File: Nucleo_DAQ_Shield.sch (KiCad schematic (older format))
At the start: 23 parts, among them J1 CONN_01X02, J2 CONN_COAXIAL, J3 CONN_01X06, J4 CONN_01X02, J5 CONN_01X06, U1 TL072, U2 7805, U3 TLV70233DBV, U4 4050

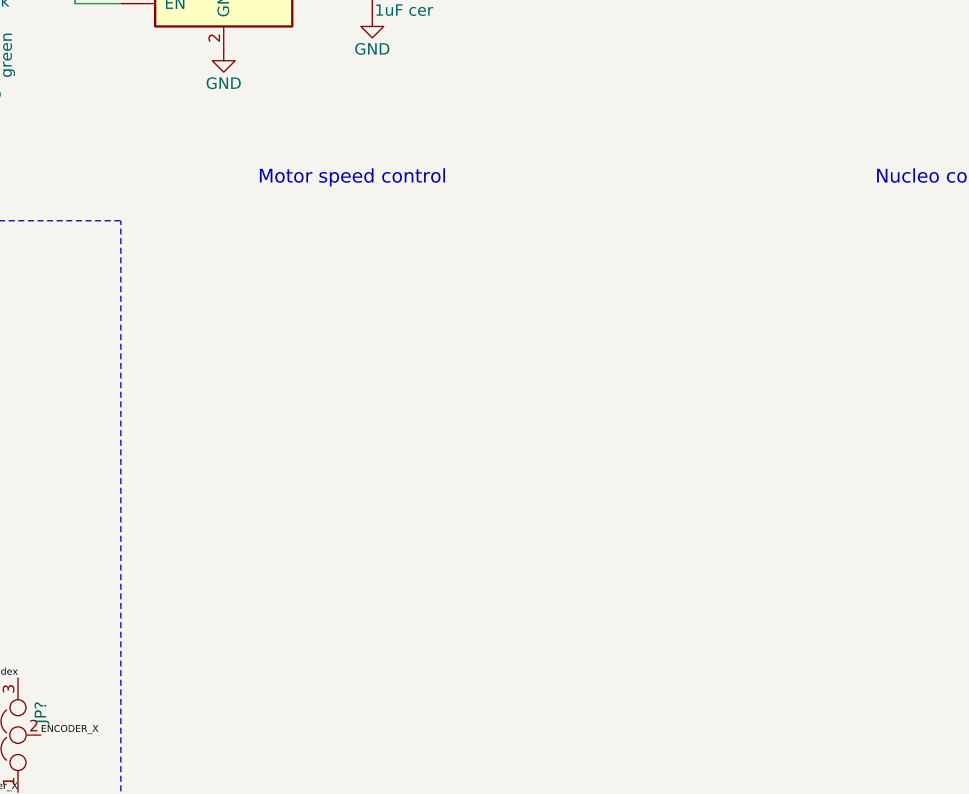
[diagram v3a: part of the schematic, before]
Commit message: Added H-bridge for motor speed control
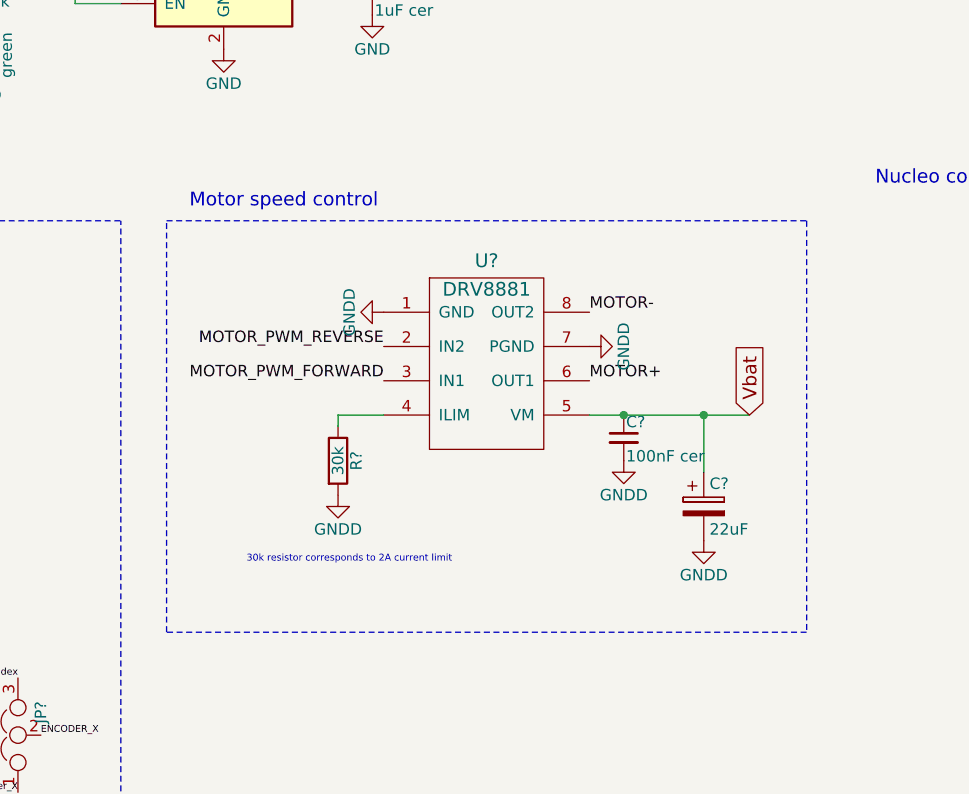
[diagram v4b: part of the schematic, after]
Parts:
- added C?: 22uF, symbol CP
- added C?: 100nF cer, symbol C_Small
- added R?: 30k, symbol R
- added U?: DRV8881, symbol DRV8881
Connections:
- net GND: now also C?.2, C?.2, R?.2, U?.1 (GND), U?.7 (PGND)
- net MOTOR+: now also U?.6 (OUT1)
- net MOTOR-: now also U?.8 (OUT2)
- net Vbat: now also C?.1, C?.1, U?.5 (VM)
- new net: R?.1, U?.4 (ILIM)
- new net MOTOR_PWM_FORWARD: U?.3 (IN1)
- new net MOTOR_PWM_REVERSE: U?.2 (IN2)
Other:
- note added: "30k resistor corresponds to 2A current limit"
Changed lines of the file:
@@
 LIBS:contrib
 LIBS:valves
+LIBS:DRV8881
 LIBS:Nucleo_DAQ_Shield-cache
 EELAYER 25 0
@@
 Text Label 4450 4350 0    30   ~ 0
 ENCODER_B
-Text Notes 6100 1950 0    60   ~ 0
+Text Notes 5800 2050 0    60   ~ 0
 Motor speed control
 Text Notes 8800 1950 0    60   ~ 0
@@
 Wire Notes Line
 	5500 5100 5500 2100
+$Comp
+L DRV8881 U?
+U 1 1 595E1ABC
+P 7100 2750
+F 0 "U?" H 7100 3225 60  0000 C CNN
+F 1 "DRV8881" H 7100 3100 60  0000 C CNN
+F 2 "" H 7100 2750 60  0001 C CNN
+F 3 "" H 7100 2750 60  0001 C CNN
+	1    7100 2750
+	1    0    0    -1
+$EndComp
+$Comp
+L GNDD #PWR?
+U 1 1 595E2075
+P 6650 2500
+F 0 "#PWR?" H 6650 2250 50  0001 C CNN
+F 1 "GNDD" H 6650 2350 50  0000 C CNN
+F 2 "" H 6650 2500 50  0001 C CNN
+F 3 "" H 6650 2500 50  0001 C CNN
+	1    6650 2500
+	0    1    1    0
+$EndComp
+$Comp
+L GNDD #PWR?
+U 1 1 595E228B
+P 7550 2650
+F 0 "#PWR?" H 7550 2400 50  0001 C CNN
+F 1 "GNDD" H 7550 2500 50  0000 C CNN
+F 2 "" H 7550 2650 50  0001 C CNN
+F 3 "" H 7550 2650 50  0001 C CNN
+	1    7550 2650
+	0    -1   -1   0
+$EndComp
+$Comp
+L CP C?
+U 1 1 595E27CD
+P 8050 3350
+F 0 "C?" H 8075 3450 50  0000 L CNN
+F 1 "22uF" H 8075 3250 50  0000 L CNN
+F 2 "" H 8088 3200 50  0001 C CNN
+F 3 "" H 8050 3350 50  0001 C CNN
+	1    8050 3350
+	1    0    0    -1
+$EndComp
+Text GLabel 8250 2950 1    60   Input ~ 0
+Vbat
+$Comp
+L R R?
+U 1 1 595E2B28
+P 6450 3150
+F 0 "R?" V 6530 3150 50  0000 C CNN
+F 1 "30k" V 6450 3150 50  0000 C CNN
+F 2 "" V 6380 3150 50  0001 C CNN
+F 3 "" H 6450 3150 50  0001 C CNN
+	1    6450 3150
+	1    0    0    -1
+$EndComp
+$Comp
+L GNDD #PWR?
+U 1 1 595E2DB5
+P 6450 3300
+F 0 "#PWR?" H 6450 3050 50  0001 C CNN
+F 1 "GNDD" H 6450 3150 50  0000 C CNN
+F 2 "" H 6450 3300 50  0001 C CNN
+F 3 "" H 6450 3300 50  0001 C CNN
+	1    6450 3300
+	1    0    0    -1
+$EndComp
+Wire Wire Line
+	6650 2950 6450 2950
+Wire Wire Line
+	6450 2950 6450 3000
+Text Label 7550 2800 0    50   ~ 0
+MOTOR+
+Text Label 7550 2500 0    50   ~ 0
+MOTOR-
+$Comp
+L C_Small C?
+U 1 1 595E32FF
+P 7700 3050
+F 0 "C?" H 7710 3120 50  0000 L CNN
+F 1 "100nF cer" H 7710 2970 50  0000 L CNN
+F 2 "" H 7700 3050 50  0001 C CNN
+F 3 "" H 7700 3050 50  0001 C CNN
+	1    7700 3050
+	1    0    0    -1
+$EndComp
+$Comp
+L GNDD #PWR?
+U 1 1 595E3B16
+P 7700 3150
+F 0 "#PWR?" H 7700 2900 50  0001 C CNN
+F 1 "GNDD" H 7700 3000 50  0000 C CNN
+F 2 "" H 7700 3150 50  0001 C CNN
+F 3 "" H 7700 3150 50  0001 C CNN
+	1    7700 3150
+	1    0    0    -1
+$EndComp
+$Comp
+L GNDD #PWR?
+U 1 1 595E3B7B
+P 8050 3500
+F 0 "#PWR?" H 8050 3250 50  0001 C CNN
+F 1 "GNDD" H 8050 3350 50  0000 C CNN
+F 2 "" H 8050 3500 50  0001 C CNN
+F 3 "" H 8050 3500 50  0001 C CNN
+	1    8050 3500
+	1    0    0    -1
+$EndComp
+Wire Wire Line
+	7550 2950 8250 2950
+Connection ~ 7700 2950
+Connection ~ 8050 2950
+Text Label 6650 2800 2    50   ~ 0
+MOTOR_PWM_FORWARD
+Text Label 6650 2650 2    50   ~ 0
+MOTOR_PWM_REVERSE
+Wire Wire Line
+	8050 3200 8050 2950
+Text Notes 6050 3600 0    30   ~ 0
+30k resistor corresponds to 2A current limit
+Wire Notes Line
+	5700 2100 8500 2100
+Wire Notes Line
+	8500 2100 8500 3900
+Wire Notes Line
+	8500 3900 5700 3900
+Wire Notes Line
+	5700 3900 5700 2100
 $EndSCHEMATC

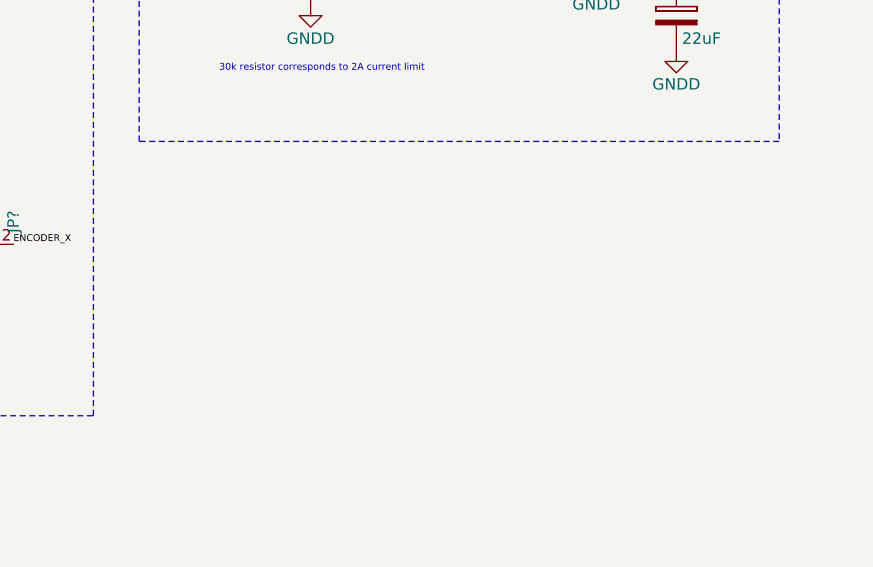
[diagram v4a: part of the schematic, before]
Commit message: Added reference diagram for the electrical characteristics of the ADC input
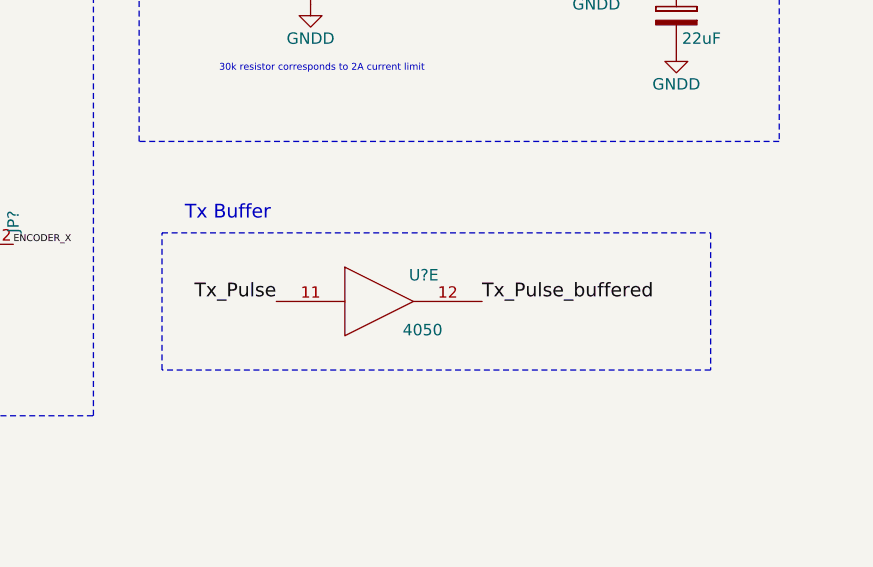
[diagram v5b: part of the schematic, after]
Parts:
- added U?: 4050, symbol 4050
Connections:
- net +3.3VA: now also U?.1 (VCC)
- net GND: now also U?.8 (VSS)
- new net Tx_Pulse: U?.11
- new net Tx_Pulse_buffered: U?.12
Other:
- note added: "Tx Buffer"

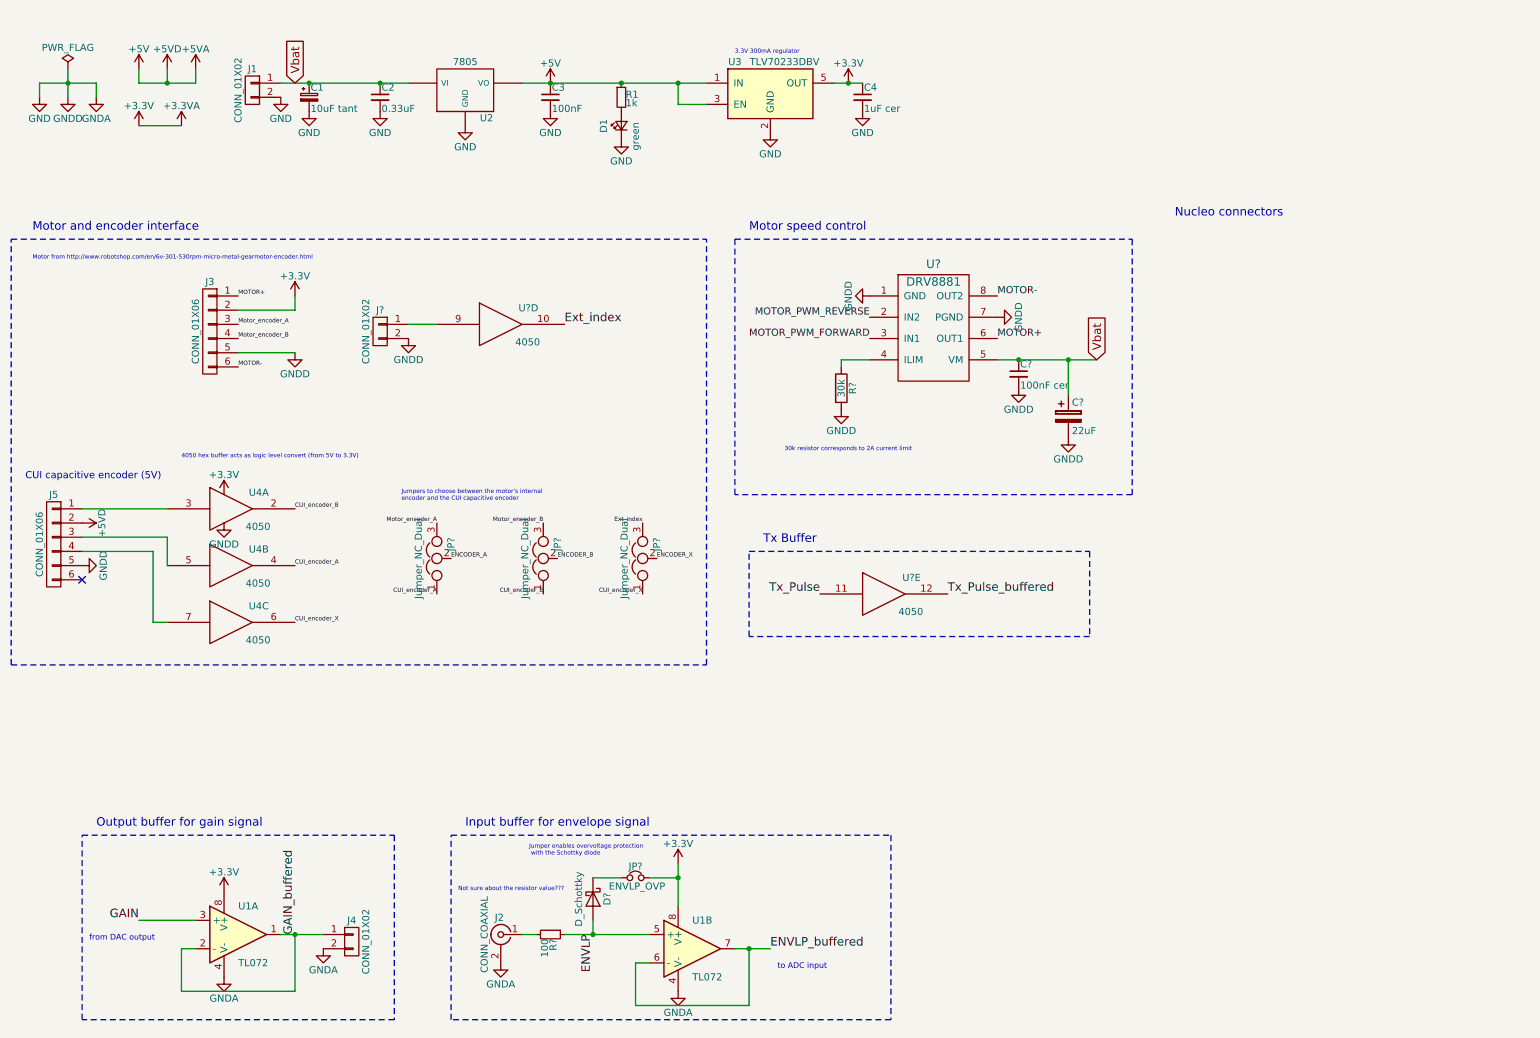
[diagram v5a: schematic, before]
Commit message: Added Nucleo connectors to schematic and started associating footprints
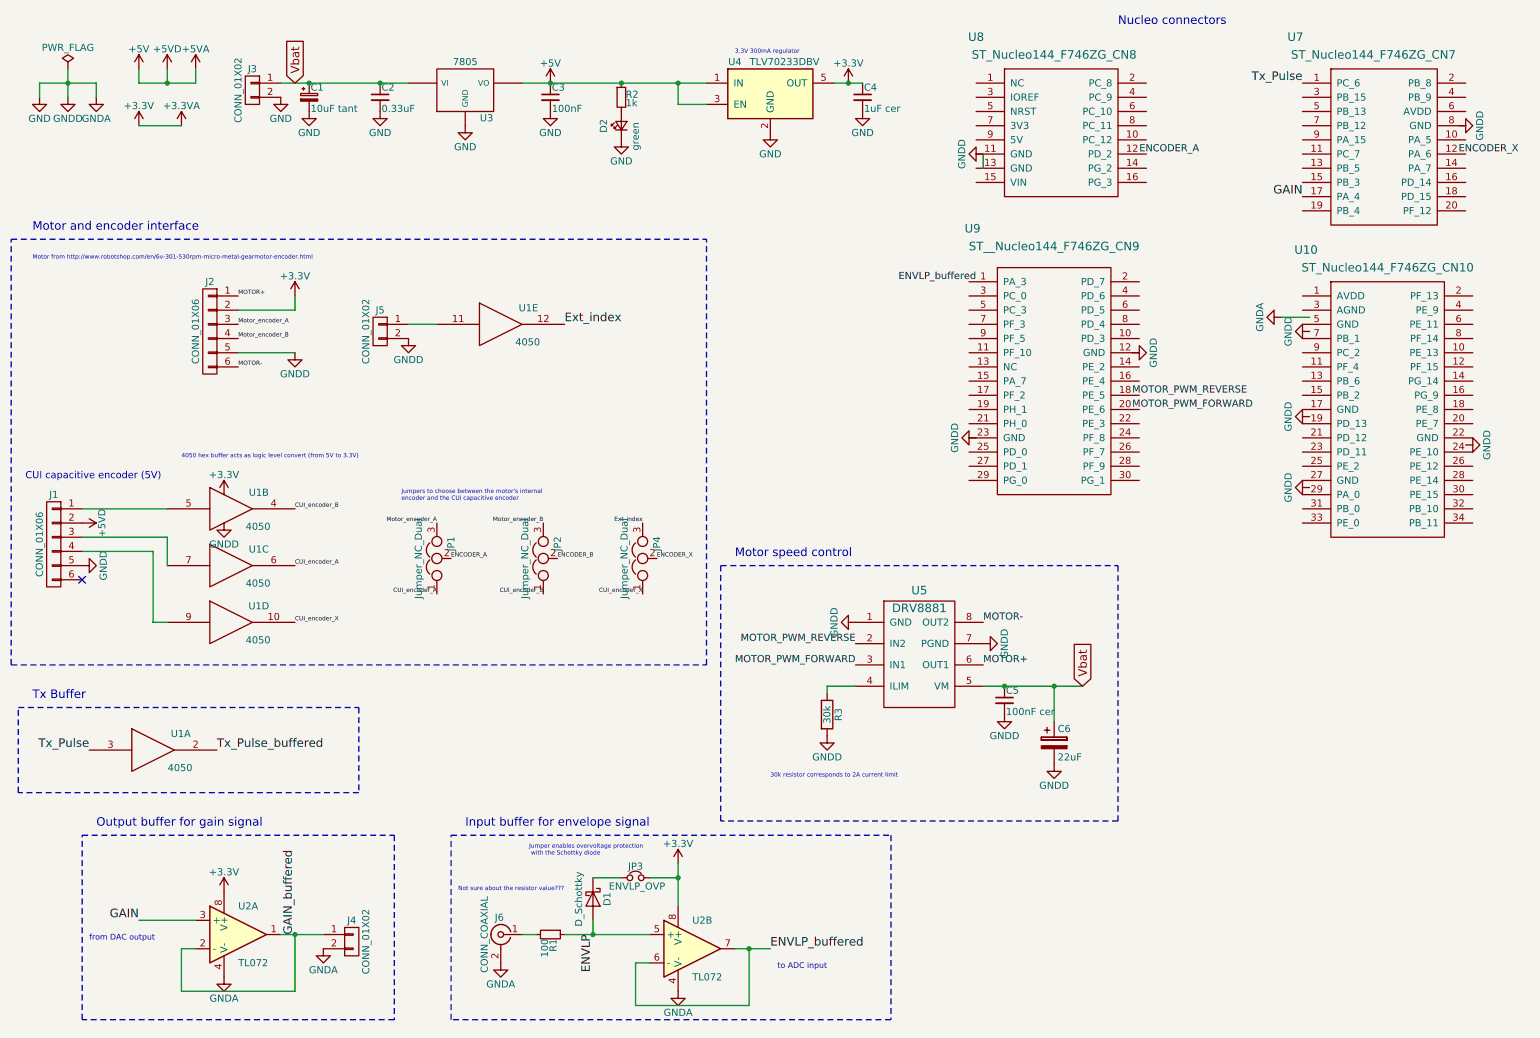
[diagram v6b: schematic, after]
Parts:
- added U10: ST_Nucleo144_F746ZG_CN10, symbol ST_Nucleo144_F746ZG_CN10
- added U7: ST_Nucleo144_F746ZG_CN7, symbol ST_Nucleo144_F746ZG_CN7
- added U8: ST_Nucleo144_F746ZG_CN8, symbol ST_Nucleo144_F746ZG_CN8
- added U9: ST__Nucleo144_F746ZG_CN9, symbol ST__Nucleo144_F746ZG_CN9
- gave numbers to parts that had none: 12
- renumbered D1 to D2, J5 to J1, J3 to J2, J1 to J3, J2 to J6, R1 to R2, U4 to U1, U1 to U2, U2 to U3, U3 to U4
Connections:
- wire segments 45 -> 47
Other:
- moved on the sheet: C5, C6, R3, U5
